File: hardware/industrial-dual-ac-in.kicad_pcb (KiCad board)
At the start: 2 copper layers, 40 x 40 mm, 30 parts, among them P1 CON-SENSOR2, P2 BOOT, P3 Debug, P4 Input, U1 XMC1100, U109 HCPL2731

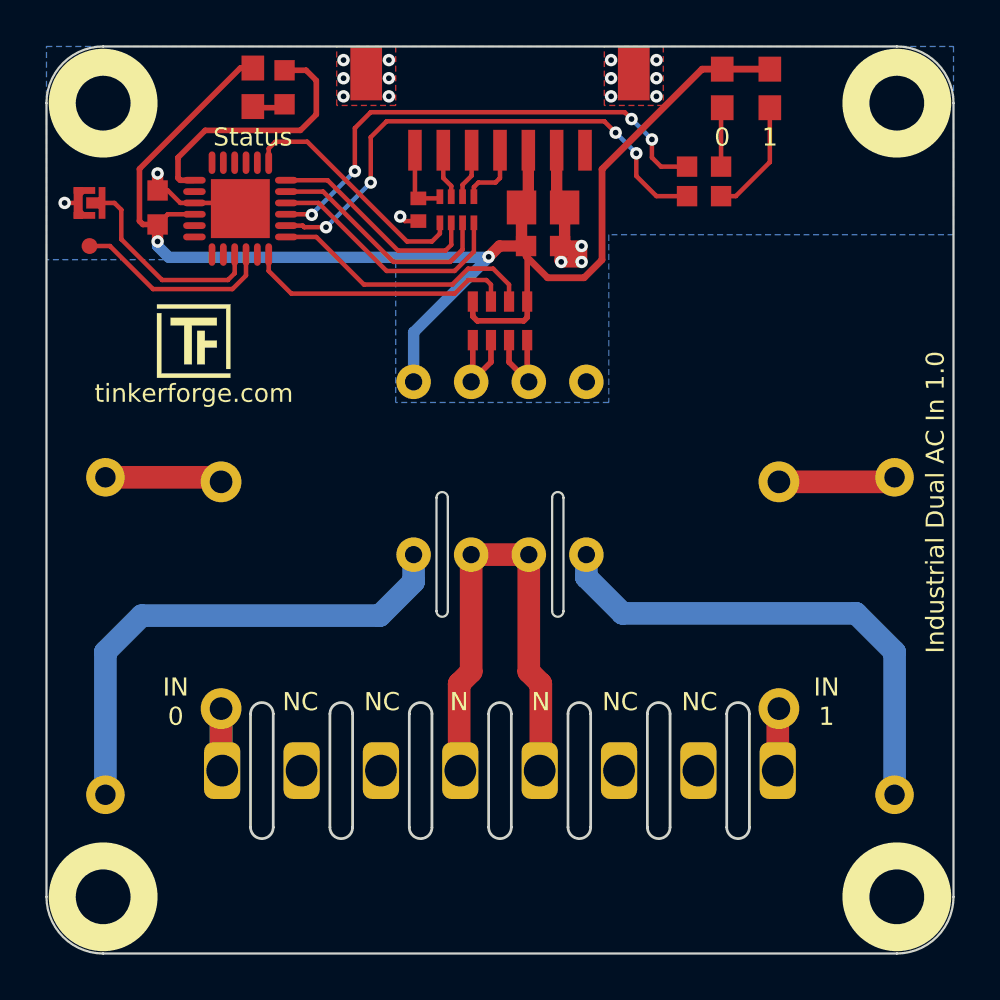
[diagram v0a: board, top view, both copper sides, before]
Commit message: more clearance for screwholes
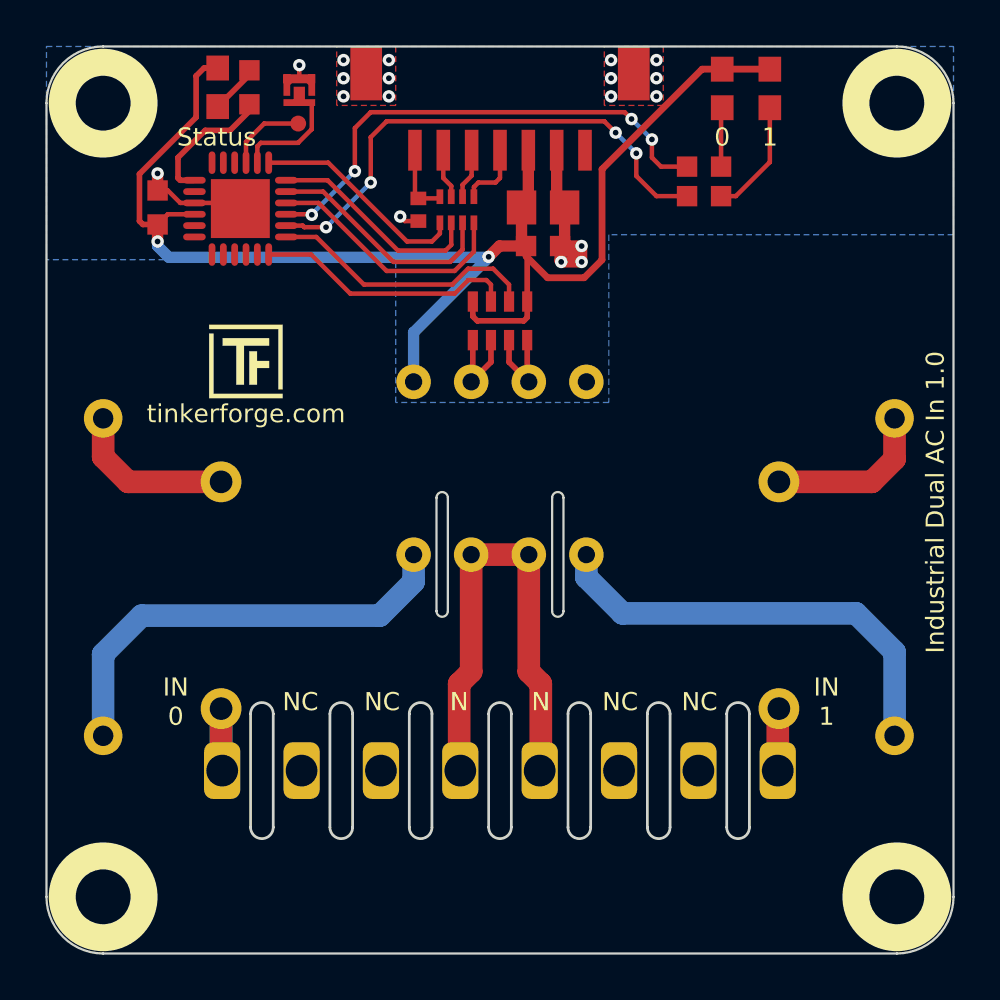
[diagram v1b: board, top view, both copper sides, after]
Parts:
- moved P3 10.7 mm to (111.1, 63.4)
- moved P2 10.5 mm to (111.2, 61.9), turned to -90 degrees
- moved R118 2.60 mm to (102.5, 83.4)
- moved R116 2.60 mm to (137.4, 83.4)
- moved G*** 2.47 mm to (108.8, 73.9)
- moved VAL 1.96 mm to (106.3, 74.3)
- moved VAL 1.96 mm to (112.3, 74.0)
- moved D1 1.55 mm to (107.5, 61.8)
- moved R1 1.55 mm to (109.0, 61.8), turned to 90 degrees
- moved G*** 0.73 mm to (132.0, 74.0)
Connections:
- U1 pad 15: Net-(P2-Pad2) -> unconnected-(U1-Pad15)
- U1 pad 16: Net-(P3-Pad1) -> unconnected-(U1-Pad16)
- U1 pad 2: unconnected-(U1-Pad2) -> Net-(P2-Pad2)
- U1 pad 3: unconnected-(U1-Pad3) -> Net-(P3-Pad1)
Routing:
- net Net-(R1-Pad1): track 11.6 -> 6.18 mm
- net Net-(P3-Pad1): track 8.86 -> 3.56 mm
- net Net-(P2-Pad2): track 8.97 -> 5.16 mm
- net Net-(R116-Pad2): track 22.3 -> 19.7 mm
- net Net-(R118-Pad2): track 22.4 -> 19.8 mm
- net Net-(D115-Pad2): track 5.18 -> 7.36 mm
- net Net-(D116-Pad2): track 5.18 -> 7.31 mm
- net S-MISO: track 10.7 -> 9.61 mm
- net Net-(D1-Pad2): track 1.57 -> 2.53 mm

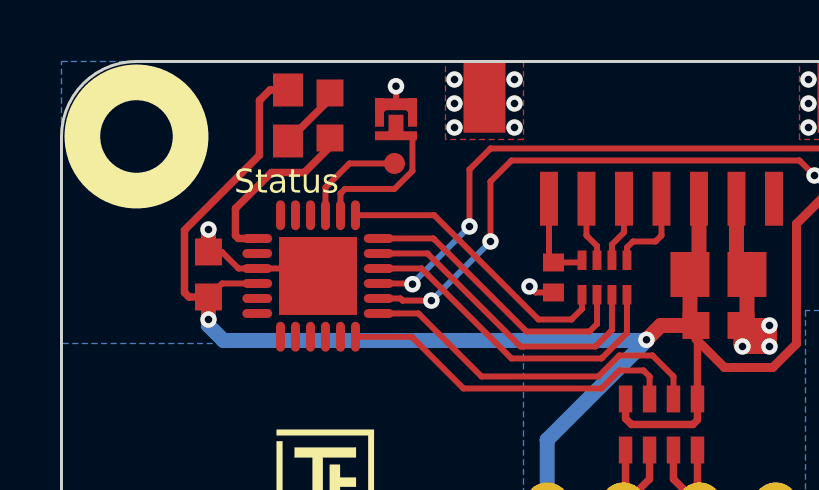
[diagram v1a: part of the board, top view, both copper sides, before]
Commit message: switched debug an boot pin
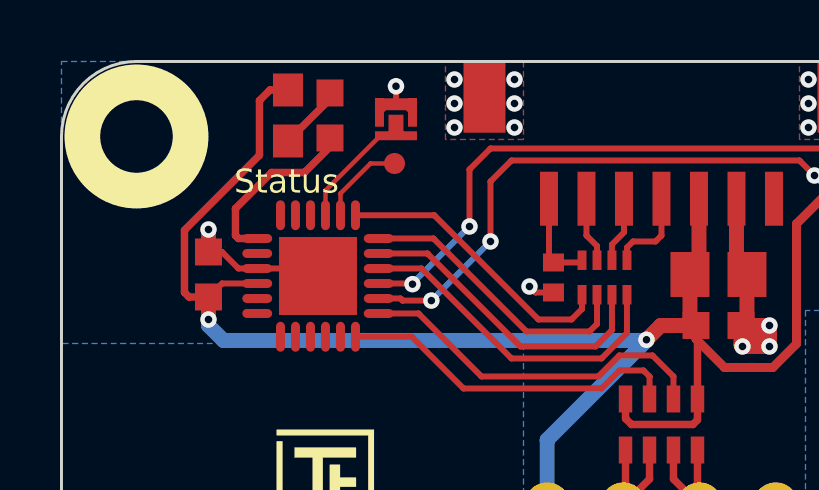
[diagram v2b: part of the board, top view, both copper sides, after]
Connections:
- P2 pad 2: Net-(P2-Pad2) -> Net-(U1-Pad3)
- P3 pad 1: Net-(P3-Pad1) -> Net-(U1-Pad2)
- U1 pad 2: Net-(P2-Pad2) -> Net-(U1-Pad2)
- U1 pad 3: Net-(P3-Pad1) -> Net-(U1-Pad3)
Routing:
- net Net-(P2-Pad2): track 5.16 -> 0.00 mm
- net Net-(U1-Pad3): track 0.00 -> 3.93 mm
- net Net-(P3-Pad1): track 3.56 -> 0.00 mm
- net Net-(U1-Pad2): track 0.00 -> 2.94 mm
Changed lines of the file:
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@@
   (net 11 "Net-(P1-Pad5)")
   (net 12 "Net-(P1-Pad6)")
-  (net 13 "Net-(P2-Pad2)")
-  (net 14 "Net-(P3-Pad1)")
+  (net 13 "Net-(U1-Pad3)")
+  (net 14 "Net-(U1-Pad2)")
   (net 15 "unconnected-(P4-Pad2)")
   (net 16 "unconnected-(P4-Pad3)")
@@
     )
     (pad "1" smd circle locked (at 0 0) (size 0.7 0.7) (layers "F.Cu" "F.Paste" "F.Mask")
-      (net 14 "Net-(P3-Pad1)") (pinfunction "P1") (pintype "passive"))
+      (net 14 "Net-(U1-Pad2)") (pinfunction "P1") (pintype "passive"))
   )
   (footprint "kicad-libraries:QFN24-4x4mm-0.5mm" (layer "F.Cu")
@@
       (net 23 "S-MISO") (pinfunction "P2.0_AIO") (pintype "passive"))
     (pad "2" smd oval locked (at -2.025 -0.75 270) (size 1 0.3) (layers "F.Cu" "F.Paste" "F.Mask")
-      (net 13 "Net-(P2-Pad2)") (pinfunction "P2.1_AIO") (pintype "passive"))
+      (net 14 "Net-(U1-Pad2)") (pinfunction "P2.1_AIO") (pintype "passive"))
     (pad "3" smd oval locked (at -2.025 -0.25 270) (size 1 0.3) (layers "F.Cu" "F.Paste" "F.Mask")
-      (net 14 "Net-(P3-Pad1)") (pinfunction "P2.2_AI") (pintype "passive"))
+      (net 13 "Net-(U1-Pad3)") (pinfunction "P2.2_AI") (pintype "passive"))
     (pad "4" smd oval locked (at -2.025 0.25 270) (size 1 0.3) (layers "F.Cu" "F.Paste" "F.Mask")
       (net 33 "unconnected-(U1-Pad4)") (pinfunction "P2.6_AI") (pintype "passive+no_connect"))
@@
       (net 2 "GND") (pinfunction "P1") (pintype "passive"))
     (pad "2" smd rect locked (at 0.55 0 270) (size 0.3 1.4) (layers "F.Cu" "F.Mask")
-      (net 13 "Net-(P2-Pad2)") (pinfunction "P2") (pintype "passive"))
+      (net 13 "Net-(U1-Pad3)") (pinfunction "P2") (pintype "passive"))
     (pad "2" smd rect locked (at 0.15 0 270) (size 0.6 0.5) (layers "F.Cu" "F.Mask")
-      (net 13 "Net-(P2-Pad2)") (pinfunction "P2") (pintype "passive"))
+      (net 13 "Net-(U1-Pad3)") (pinfunction "P2") (pintype "passive"))
   )
   (footprint "kicad-libraries:Logo_31x31" (layer "F.Cu")
@@
   (segment (start 117.5 65.8) (end 117.5 64.575) (width 0.2) (layer "F.Cu") (net 12))
   (segment (start 117.85108 66.625) (end 117.85108 66.15108) (width 0.2) (layer "F.Cu") (net 12))
-  (segment (start 111.699 63.648114) (end 111.699 62.475) (width 0.2) (layer "F.Cu") (net 13))
-  (segment (start 109.3 64.4) (end 109.451 64.249) (width 0.2) (layer "F.Cu") (net 13))
-  (segment (start 111.699 62.475) (end 111.15 62.475) (width 0.2) (layer "F.Cu") (net 13))
-  (segment (start 109.451 64.249) (end 111.098114 64.249) (width 0.2) (layer "F.Cu") (net 13))
-  (segment (start 111.098114 64.249) (end 111.699 63.648114) (width 0.2) (layer "F.Cu") (net 13))
-  (segment (start 109.3 65.125) (end 109.3 64.4) (width 0.2) (layer "F.Cu") (net 13))
-  (segment (start 109.6 63.4) (end 108.8 64.2) (width 0.2) (layer "F.Cu") (net 14))
-  (segment (start 108.8 64.2) (end 108.8 65.125) (width 0.2) (layer "F.Cu") (net 14))
-  (segment (start 111.1 63.4) (end 109.6 63.4) (width 0.2) (layer "F.Cu") (net 14))
+  (segment (start 108.8 64.3) (end 110.625 62.475) (width 0.15) (layer "F.Cu") (net 13))
+  (segment (start 110.625 62.475) (end 111.15 62.475) (width 0.15) (layer "F.Cu") (net 13))
+  (segment (start 108.8 65.125) (end 108.8 64.3) (width 0.15) (layer "F.Cu") (net 13))
+  (segment (start 110.3 63.4) (end 109.3 64.4) (width 0.15) (layer "F.Cu") (net 14))
+  (segment (start 111.1 63.4) (end 110.3 63.4) (width 0.15) (layer "F.Cu") (net 14))
+  (segment (start 109.3 64.4) (end 109.3 65.125) (width 0.15) (layer "F.Cu") (net 14))
   (segment (start 118.2 91.88431) (end 118.2 88.1) (width 1) (layer "F.Cu") (net 17))
   (segment (start 118.24994 91.93425) (end 118.2 91.88431) (width 1) (layer "F.Cu") (net 17))

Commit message: added fiducial mark
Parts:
- added Fiducial_Mark: VAL**, kicad-libraries:Fiducial_Mark, F.Cu at (108.0, 98.0)
- added Fiducial_Mark: VAL**, kicad-libraries:Fiducial_Mark, F.Cu at (134.0, 66.0)
- added Fiducial_Mark: VAL**, kicad-libraries:Fiducial_Mark, F.Cu at (102.0, 68.0)
- added Fiducial_Mark: VAL**, kicad-libraries:Fiducial_Mark, F.Cu at (132.0, 98.0)
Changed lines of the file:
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@@
       (outputformat 1)
       (mirror false)
-      (drillshape 1)
+      (drillshape 0)
       (scaleselection 1)
-      (outputdirectory "")
+      (outputdirectory "Ind-dual-ac-in-gerber/")
     )
   )
@@
     )
   )
+  (footprint "kicad-libraries:Fiducial_Mark" (layer "F.Cu")
+    (at 108 98)
+    (attr smd)
+    (fp_text reference "Fiducial_Mark" (at 0 0) (layer "F.SilkS") hide
+      (effects (font (size 0.127 0.127) (thickness 0.03302)))
+    )
+    (fp_text value "VAL**" (at 0 -0.29972) (layer "F.SilkS") hide
+      (effects (font (size 0.127 0.127) (thickness 0.03302)))
+    )
+    (fp_circle (center 0 0) (end 1.15062 0) (layer "Dwgs.User") (width 0.01016) (fill none))
+    (pad "1" smd circle locked (at 0 0) (size 1.00076 1.00076) (layers "F.Cu" "F.Paste" "F.Mask")
+      (clearance 0.65024))
+  )
+  (footprint "kicad-libraries:Fiducial_Mark" (layer "F.Cu")
+    (at 134 66)
+    (attr smd)
+    (fp_text reference "Fiducial_Mark" (at 0 0) (layer "F.SilkS") hide
+      (effects (font (size 0.127 0.127) (thickness 0.03302)))
+    )
+    (fp_text value "VAL**" (at 0 -0.29972) (layer "F.SilkS") hide
+      (effects (font (size 0.127 0.127) (thickness 0.03302)))
+    )
+    (fp_circle (center 0 0) (end 1.15062 0) (layer "Dwgs.User") (width 0.01016) (fill none))
+    (pad "1" smd circle locked (at 0 0) (size 1.00076 1.00076) (layers "F.Cu" "F.Paste" "F.Mask")
+      (clearance 0.65024))
+  )
   (footprint "kicad-libraries:DO-41" (layer "F.Cu")
     (at 132.3 84.2 90)
@@
       (rotate (xyz 0 0 0))
     )
+  )
+  (footprint "kicad-libraries:Fiducial_Mark" (layer "F.Cu")
+    (at 102 68)
+    (attr smd)
+    (fp_text reference "Fiducial_Mark" (at 0 0) (layer "F.SilkS") hide
+      (effects (font (size 0.127 0.127) (thickness 0.03302)))
+    )
+    (fp_text value "VAL**" (at 0 -0.29972) (layer "F.SilkS") hide
+      (effects (font (size 0.127 0.127) (thickness 0.03302)))
+    )
+    (fp_circle (center 0 0) (end 1.15062 0) (layer "Dwgs.User") (width 0.01016) (fill none))
+    (pad "1" smd circle locked (at 0 0) (size 1.00076 1.00076) (layers "F.Cu" "F.Paste" "F.Mask")
+      (clearance 0.65024))
   )
   (footprint "kicad-libraries:OQ_8P_230V" (layer "F.Cu")
@@
     )
   )
+  (footprint "kicad-libraries:Fiducial_Mark" (layer "F.Cu")
+    (at 132 98)
+    (attr smd)
+    (fp_text reference "Fiducial_Mark" (at 0 0) (layer "F.SilkS") hide
+      (effects (font (size 0.127 0.127) (thickness 0.03302)))
+    )
+    (fp_text value "VAL**" (at 0 -0.29972) (layer "F.SilkS") hide
+      (effects (font (size 0.127 0.127) (thickness 0.03302)))
+    )
+    (fp_circle (center 0 0) (end 1.15062 0) (layer "Dwgs.User") (width 0.01016) (fill none))
+    (pad "1" smd circle locked (at 0 0) (size 1.00076 1.00076) (layers "F.Cu" "F.Paste" "F.Mask")
+      (clearance 0.65024))
+  )
   (footprint "kicad-libraries:D0603E" (layer "F.Cu")
